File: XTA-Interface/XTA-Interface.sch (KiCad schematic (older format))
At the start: 23 parts, among them J1 IDE_CONNECTOR, J2 CF Adapter Power, J3 Bus_ISA_8bit, J4 Addresses, J5 Addresses, U1 BIOS FLASH, U2 74HCT245, U3 ATF/GAL22V10x-15, U4 DS1315, U5 AS6C4008-55PCN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

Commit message: WIP on XTA interface card.
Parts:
- removed BAT1: CR2032, Battery:BatteryHolder_Keystone_103_1x20mm, symbol Device:Battery_Cell
- removed C6: 0.1uF, Capacitor_THT:C_Disc_D6.0mm_W2.5mm_P5.00mm, symbol Device:C
- removed H1, H2, H3, H4: MountingHole_Pad, MountingHole:MountingHole_3.5mm_Pad, symbol Mechanical:MountingHole_Pad
- removed J2: CF Adapter Power, Connector_PinSocket_2.54mm:PinSocket_1x02_P2.54mm_Vertical, symbol Connector_Generic:Conn_01x02
- removed U4: DS1315, Package_DIP:DIP-16_W7.62mm_Socket, symbol 00Common:DS1315
- removed U5: AS6C4008-55PCN, Package_DIP:DIP-32_W15.24mm_Socket, symbol Memory_RAM:AS6C4008-55PCN
- removed Y1: 32.768 KHz, Crystal:Crystal_C38-LF_D3.0mm_L8.0mm_Horizontal, symbol Device:Crystal
- added J2: Drive Power, Connector_PinHeader_2.54mm:PinHeader_1x06_P2.54mm_Horizontal, symbol Connector_Generic:Conn_01x06
- added J6: LEDs, Connector_PinHeader_2.54mm:PinHeader_1x04_P2.54mm_Horizontal, symbol Connector_Generic:Conn_01x04
- added J7: XTA_CONNECTOR_1, Connector_PinHeader_2.54mm:PinHeader_2x20_P2.54mm_Vertical, symbol 00Common:XTA_CONNECTOR
- added R1: 1K, Resistor_SMD:R_1206_3216Metric, symbol Device:R
- added U4: 74LS14, Package_DIP:DIP-14_W7.62mm_Socket, symbol 74xx:74LS14
- added U5: 74LS00, Package_DIP:DIP-14_W7.62mm_Socket, symbol 74xx:74LS00
- C1, C2, C3, C4, C5: footprint Capacitor_THT:C_Disc_D6.0mm_W2.5mm_P5.00mm -> Capacitor_SMD:C_1206_3216Metric
- C6: renamed from C7; value 22uF -> 22uF 25v; footprint Capacitor_THT:CP_Radial_D5.0mm_P2.50mm -> Capacitor_Tantalum_SMD:CP_EIA-3528-15_AVX-H
- J1: value IDE_CONNECTOR -> XTA_CONNECTOR_0; footprint Connector_PinSocket_2.54mm:PinSocket_2x20_P2.54mm_Vertical -> Connector_PinHeader_2.54mm:PinHeader_2x20_P2.54mm_Vertical; symbol 00Common:IDE_CONNECTOR -> 00Common:XTA_CONNECTOR
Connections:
- net labels added: +12V, AEN, BIOS_SEL_JUMPER, IRQ2, IRQ5, ROM_ADDR_JUMPER_0, ROM_ADDR_JUMPER_1, XTA_DRQ, XTA_IRQ, ~CS_XTA0, ~CS_XTA1, ~DACK3, ~DRV_ACTIVE, ~XTA_DACK
- net labels removed: ATA_ADDR_JUMPER, ROM_ADDR_JUMPER, V20_JUMPER, XTAL1, XTAL2, ~CE~_BIOS_DECODE, ~CE~_BIOS_THRU, ~CS1~_ATA, ~IOR_OR_MEMR, ~IOR~_DELAYED, ~RESET
- wire segments 114 -> 186
- no-connect marks 39 -> 27
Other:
- note added: "0"
- note added: "1"
- note added: "1\n"
- note added: "OTHER HEADERS"
- note added: "Q"
- note added: "When ~R~ goes low, ~S~ also goes high, Q = 0\nIf ~R~ goes high, again, Q = 1\nIf ~DACK3~ is high but either of ~IOR~ or ~IOW~ go low, the state of the flop flop does not change?"
- note added: "XTA CONNECTOR"
- note added: "~R"
- note added: "~S"
- note removed: "CF ADAPTER"
- note removed: "REAL TIME CLOCK\n(OPTIONAL)"
- note removed: "TANDY 1000 SRAM\n(OPTIONAL)"
- moved on the sheet: C6

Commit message: WIP on XTA interface card.
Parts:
- removed C5: 0.1uF, Capacitor_SMD:C_1206_3216Metric, symbol Device:C
- removed U4: 74LS14, Package_DIP:DIP-14_W7.62mm_Socket, symbol 74xx:74LS14
- removed U5: 74LS00, Package_DIP:DIP-14_W7.62mm_Socket, symbol 74xx:74LS00
- added U4: ATF/GAL16V8-15, Package_DIP:DIP-20_W7.62mm_Socket, symbol 00Common:GAL16V8
- U3: value ATF/GAL22V10x-15 -> ATF/GAL16V8-15; footprint Package_DIP:DIP-24_W7.62mm_Socket -> Package_DIP:DIP-20_W7.62mm_Socket; symbol 00Common:GAL22V10 -> 00Common:GAL16V8
- renumbered C6 to C5
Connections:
- net +12V: now also J2.1 (Pin_1); no longer J2.5 (Pin_5)
- net A02: now also U3.3 (I3); no longer U3.1 (I1/CLK)
- net A03: now also U4.1 (I1/CLK); no longer U3.2 (I2)
- net A04: now also U4.2 (I2); no longer U3.3 (I3)
- net A05: now also U4.3 (I3); no longer U3.4 (I4)
- net A06: now also U4.4 (I4); no longer U3.5 (I5)
- net A07: now also U4.5 (I5); no longer U3.6 (I6)
- net A08: now also U4.6 (I6); no longer U3.7 (I7)
- net A09: now also U4.7 (I7); no longer U3.8 (I8)
- net A13: now also U3.4 (I4); no longer U3.9 (I9)
- net A14: now also U3.5 (I5); no longer U3.10 (I10)
- net A15: now also U3.6 (I6); no longer U3.11 (I11)
- net A16: now also U3.7 (I7); no longer U3.13 (I12)
- net A17: now also U3.8 (I8); no longer U3.14 (IO10)
- net A18: now also U3.9 (I9); no longer U3.15 (IO9)
- net A19: now also U3.11 (I10/~OE~); no longer U3.16 (IO8)
- net GND: now also J2.5 (Pin_5), U3.10 (GND), U4.10 (GND); no longer J2.4 (Pin_4), U3.12 (GND)
- net VCC: now also J2.3 (Pin_3), J2.4 (Pin_4), U3.20 (VCC), U4.20 (VCC); no longer J2.1 (Pin_1), U3.24 (VCC)
- net ~CE~_BIOS: now also U3.15 (IO5); no longer U3.19 (IO5)
- net ~CS_XTA0: now also U3.16 (IO4); no longer U3.20 (IO4)
- net ~CS_XTA1: now also U3.17 (I03); no longer U3.21 (I03)
- net ~DACK3: now also U4.11 (I10/~OE~)
- net ~IOR: now also U4.9 (I9)
- net ~IOW: now also U4.8 (I8)
- net ~MEMR: now also U3.13 (IO7); no longer U3.17 (IO7)
- net ~MEMR~_DELAYED: now also U3.14 (IO6); no longer U3.18 (IO6)
- net ~XTA_DACK: now also U4.12 (IO8)
- net BIOS_SEL_JUMPER renamed ST_WD_JUMPER
- net ST_WD_JUMPER: now also U3.2 (I2)
- net ROM_ADDR_JUMPER_0 renamed ADDR_JUMPER_0
- net ADDR_JUMPER_0: now also U3.19 (IO1); no longer U3.23 (IO1)
- net ROM_ADDR_JUMPER_1 renamed ADDR_JUMPER_1
- net ADDR_JUMPER_1: now also U3.18 (IO2); no longer U3.22 (IO2)
- new net DECODE_IO_RANGE: U3.1 (I1/CLK), U4.13 (IO7)
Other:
- note added: "DECODING AND GLUE"
- note added: "Spare for extra\ndelay if needed."
- note added: "Unused pins are for\nadding propogation\ndelay. Need at least 4."
- note removed: "0"
- note removed: "1"
- note removed: "1\n"
- note removed: "DECODING"
- note removed: "Q"
- note removed: "When ~R~ goes low, ~S~ also goes high, Q = 0\nIf ~R~ goes high, again, Q = 1\nIf ~DACK3~ is high but either of ~IOR~ or ~IOW~ go low, the state of the flop flop does not change?"
- note removed: "~R"
- note removed: "~S"
- moved on the sheet: U2

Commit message: More WIP on XTA interface card.
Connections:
- net A19: now also U3.14 (IO6); no longer U3.11 (I10/~OE~)
- net ADDR_JUMPER_0: now also U3.11 (I10/~OE~); no longer U3.19 (IO1)
- net ADDR_JUMPER_1: now also U3.12 (IO8); no longer U3.18 (IO2)
- net ~CE~_BIOS: now also U3.18 (IO2); no longer U3.15 (IO5)
- net ~CS_XTA0: now also U3.17 (I03); no longer U3.16 (IO4)
- net ~CS_XTA1: now also U3.16 (IO4); no longer U3.17 (I03)
- net ~MEMR: now also U3.15 (IO5); no longer U3.13 (IO7)
- net ~MEMR~_DELAYED: now also U3.19 (IO1); no longer U3.14 (IO6)
- net XTA_DRQ renamed DRQ3
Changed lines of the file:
@@
 Text GLabel 7900 4300 2    50   Input ~ 0
 D7_BUF
-Text GLabel 5250 1650 2    39   Input ~ 0
+Text GLabel 5250 1550 2    39   Input ~ 0
 ~CS_XTA0
-Text GLabel 5250 1750 2    39   Input ~ 0
+Text GLabel 5250 1450 2    39   Input ~ 0
 ~CE~_BIOS
 Text GLabel 2600 3400 2    50   Input ~ 0
@@
 Text GLabel 2600 2500 2    50   Input ~ 0
 A15
-Text GLabel 4250 2250 0    50   Input ~ 0
+Text GLabel 5250 1850 2    50   Input ~ 0
 A19
 Text GLabel 4250 2150 0    50   Input ~ 0
@@
 Text GLabel 4150 5950 0    50   Input ~ 0
 D0
-Text GLabel 5550 950  0    50   Input ~ 0
+Text GLabel 3850 2350 3    50   Input ~ 0
 ADDR_JUMPER_0
-Text GLabel 5550 850  0    50   Input ~ 0
+Text GLabel 5400 2300 3    50   Input ~ 0
 ADDR_JUMPER_1
 $Comp
@@
 XTA_IRQ
 Text GLabel 9450 2350 0    50   Input ~ 0
-XTA_DRQ
+DRQ3
 Text GLabel 9450 2250 0    39   Input ~ 0
 ~XTA_DACK
@@
 XTA_IRQ
 Text GLabel 9450 5200 0    50   Input ~ 0
-XTA_DRQ
+DRQ3
 Text GLabel 9450 5100 0    39   Input ~ 0
 ~XTA_DACK
@@
 Text GLabel 4150 6850 0    39   Input ~ 0
 ~MEMR
-Text GLabel 5250 1550 2    39   Input ~ 0
+Text GLabel 5250 1650 2    39   Input ~ 0
 ~CS_XTA1
 Text GLabel 4000 3350 0    50   Input ~ 0
@@
 Text GLabel 4250 1750 0    50   Input ~ 0
 A14
-Text GLabel 5250 1850 2    39   Input ~ 0
+Text GLabel 5250 1350 2    39   Input ~ 0
 ~MEMR~_DELAYED
-Text GLabel 5250 1950 2    39   Input ~ 0
+Text GLabel 5250 1750 2    39   Input ~ 0
 ~MEMR
 $Comp
@@
 	2500 2000 2600 2000
 Text GLabel 1000 2500 0    50   Input ~ 0
-XTA_DRQ
+DRQ3
 Text GLabel 1000 2400 0    39   Input ~ 0
 ~DACK3
@@
 Text GLabel 5000 4050 2    39   Input ~ 0
 ~XTA_DACK
-NoConn ~ 5250 2050
+NoConn ~ 5250 1950
 NoConn ~ 5000 3450
 NoConn ~ 5000 3350
@@
 Wire Wire Line
 	3700 950  3850 950
-Wire Wire Line
-	5250 1350 5650 1350
-Wire Wire Line
-	5650 1350 5650 950
-Wire Wire Line
-	5650 950  5550 950
-Wire Wire Line
-	5550 850  5750 850
-Wire Wire Line
-	5750 850  5750 1450
-Wire Wire Line
-	5750 1450 5250 1450
-Text Notes 5150 2250 0    50   ~ 0
+Text Notes 2950 2200 0    50   ~ 0
 Spare for extra\ndelay if needed.
 Text Notes 4900 4350 0    50   ~ 0
 Unused pins are for\nadding propogation\ndelay. Need at least 4.
+Wire Wire Line
+	5250 2050 5400 2050
+Wire Wire Line
+	5400 2050 5400 2300
+Wire Wire Line
+	4250 2250 3850 2250
+Wire Wire Line
+	3850 2250 3850 2350
 $EndSCHEMATC

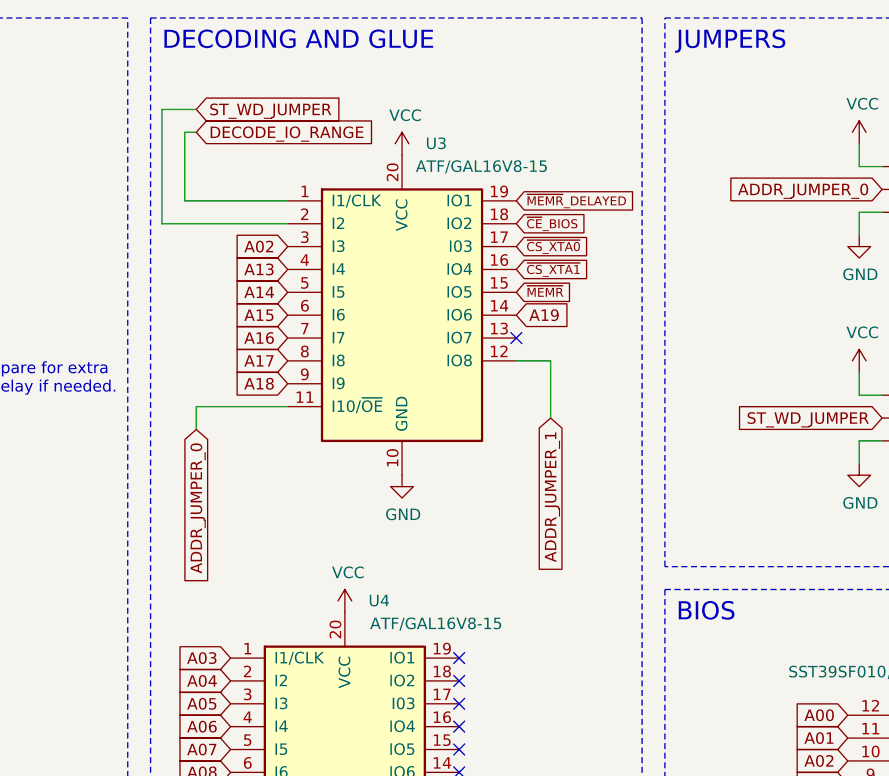
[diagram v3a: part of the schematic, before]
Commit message: XTA interface WIP. All items connected - still needs a bunch of cleanup.
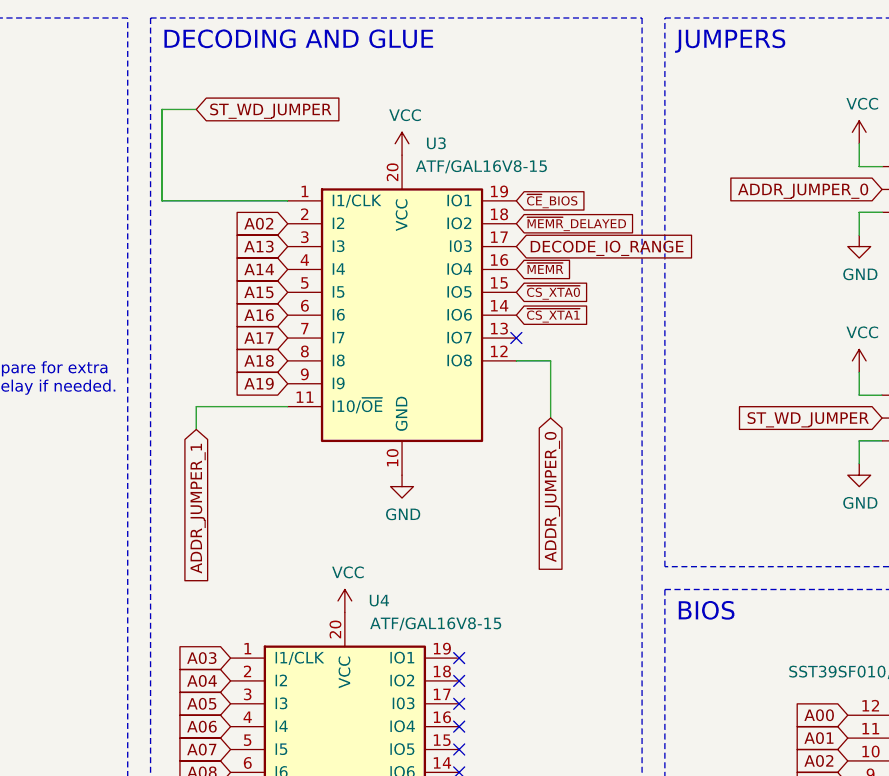
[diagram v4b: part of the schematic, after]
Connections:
- net A02: now also U3.2 (I2); no longer U3.3 (I3)
- net A13: now also U3.3 (I3); no longer U3.4 (I4)
- net A14: now also U3.4 (I4); no longer U3.5 (I5)
- net A15: now also U3.5 (I5); no longer U3.6 (I6)
- net A16: now also U3.6 (I6); no longer U3.7 (I7)
- net A17: now also U3.7 (I7); no longer U3.8 (I8)
- net A18: now also U3.8 (I8); no longer U3.9 (I9)
- net A19: now also U3.9 (I9); no longer U3.14 (IO6)
- net ADDR_JUMPER_0: now also U3.12 (IO8); no longer U3.11 (I10/~OE~)
- net ADDR_JUMPER_1: now also U3.11 (I10/~OE~); no longer U3.12 (IO8)
- net DECODE_IO_RANGE: now also U3.17 (I03); no longer U3.1 (I1/CLK)
- net ST_WD_JUMPER: now also U3.1 (I1/CLK); no longer U3.2 (I2)
- net ~CE~_BIOS: now also U3.19 (IO1); no longer U3.18 (IO2)
- net ~CS_XTA0: now also U3.15 (IO5); no longer U3.17 (I03)
- net ~CS_XTA1: now also U3.14 (IO6); no longer U3.16 (IO4)
- net ~MEMR: now also U3.16 (IO4); no longer U3.15 (IO5)
- net ~MEMR~_DELAYED: now also U3.18 (IO2); no longer U3.19 (IO1)
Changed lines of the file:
@@
 Text GLabel 7900 4300 2    50   Input ~ 0
 D7_BUF
-Text GLabel 5250 1550 2    39   Input ~ 0
+Text GLabel 5250 1750 2    39   Input ~ 0
 ~CS_XTA0
-Text GLabel 5250 1450 2    39   Input ~ 0
+Text GLabel 5250 1350 2    39   Input ~ 0
 ~CE~_BIOS
 Text GLabel 2600 3400 2    50   Input ~ 0
@@
 Text GLabel 2600 2500 2    50   Input ~ 0
 A15
-Text GLabel 5250 1850 2    50   Input ~ 0
+Text GLabel 4250 2150 0    50   Input ~ 0
 A19
-Text GLabel 4250 2150 0    50   Input ~ 0
+Text GLabel 4250 2050 0    50   Input ~ 0
 A18
-Text GLabel 4250 2050 0    50   Input ~ 0
+Text GLabel 4250 1950 0    50   Input ~ 0
 A17
-Text GLabel 4250 1950 0    50   Input ~ 0
+Text GLabel 4250 1850 0    50   Input ~ 0
 A16
-Text GLabel 4250 1850 0    50   Input ~ 0
+Text GLabel 4250 1750 0    50   Input ~ 0
 A15
 Connection ~ 6100 5400
@@
 Text GLabel 4150 5950 0    50   Input ~ 0
 D0
+Text GLabel 5400 2300 3    50   Input ~ 0
+ADDR_JUMPER_0
 Text GLabel 3850 2350 3    50   Input ~ 0
-ADDR_JUMPER_0
-Text GLabel 5400 2300 3    50   Input ~ 0
 ADDR_JUMPER_1
 $Comp
@@
 Text GLabel 4150 6850 0    39   Input ~ 0
 ~MEMR
-Text GLabel 5250 1650 2    39   Input ~ 0
+Text GLabel 5250 1850 2    39   Input ~ 0
 ~CS_XTA1
 Text GLabel 4000 3350 0    50   Input ~ 0
 A03
+Text GLabel 4250 1450 0    50   Input ~ 0
+A02
 Text GLabel 4250 1550 0    50   Input ~ 0
-A02
+A13
 Text GLabel 4250 1650 0    50   Input ~ 0
-A13
-Text GLabel 4250 1750 0    50   Input ~ 0
 A14
-Text GLabel 5250 1350 2    39   Input ~ 0
+Text GLabel 5250 1450 2    39   Input ~ 0
 ~MEMR~_DELAYED
-Text GLabel 5250 1750 2    39   Input ~ 0
+Text GLabel 5250 1650 2    39   Input ~ 0
 ~MEMR
 $Comp
@@
 Text GLabel 5000 3950 2    50   Input ~ 0
 DECODE_IO_RANGE
-Text GLabel 3850 1050 2    50   Input ~ 0
+Text GLabel 5250 1550 2    50   Input ~ 0
 DECODE_IO_RANGE
 $Comp
@@
 NoConn ~ 5000 3550
 Wire Wire Line
-	4250 1350 3800 1350
-Wire Wire Line
-	3800 1350 3800 1050
-Wire Wire Line
-	3800 1050 3850 1050
-Wire Wire Line
-	4250 1450 3700 1450
-Wire Wire Line
-	3700 1450 3700 950
-Wire Wire Line
 	3700 950  3850 950
 Text Notes 2950 2200 0    50   ~ 0
@@
 Wire Wire Line
 	3850 2250 3850 2350
+Wire Wire Line
+	4250 1350 3700 1350
+Wire Wire Line
+	3700 1350 3700 950
 $EndSCHEMATC

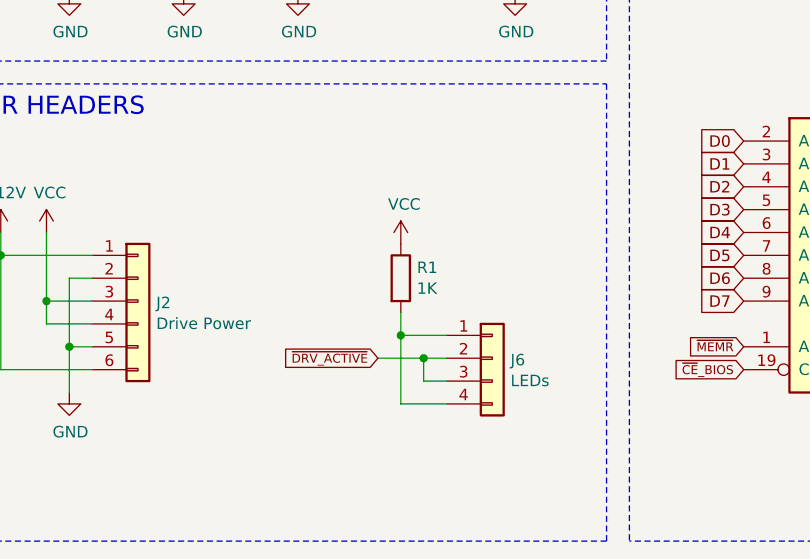
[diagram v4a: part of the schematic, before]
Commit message: WIP on XTA interface layout.
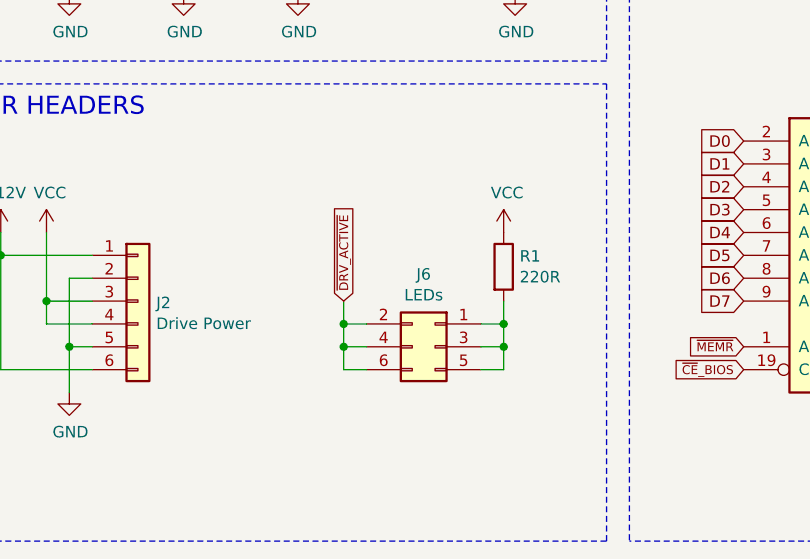
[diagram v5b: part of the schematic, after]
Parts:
- removed J6: LEDs, Connector_PinHeader_2.54mm:PinHeader_1x04_P2.54mm_Horizontal, symbol Connector_Generic:Conn_01x04
- added J6: LEDs, Connector_PinHeader_2.54mm:PinHeader_2x03_P2.54mm_Vertical, symbol Connector_Generic:Conn_02x03_Odd_Even
- R1: value 1K -> 220R
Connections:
- net ~DRV_ACTIVE: now also J6.2 (Pin_2), J6.4 (Pin_4), J6.6 (Pin_6)
- net at R1.2: now also J6.1 (Pin_1), J6.3 (Pin_3), J6.5 (Pin_5)
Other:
- moved on the sheet: R1
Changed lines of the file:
@@
 L Device:R R1
 U 1 1 6153EA2A
-P 2650 6550
-F 0 "R1" H 2720 6596 50  0000 L CNN
-F 1 "1K" H 2720 6505 50  0000 L CNN
-F 2 "Resistor_SMD:R_1206_3216Metric" V 2580 6550 50  0001 C CNN
-F 3 "~" H 2650 6550 50  0001 C CNN
-	1    2650 6550
+P 3100 6500
+F 0 "R1" H 3170 6546 50  0000 L CNN
+F 1 "220R" H 3170 6455 50  0000 L CNN
+F 2 "Resistor_SMD:R_1206_3216Metric" V 3030 6500 50  0001 C CNN
+F 3 "~" H 3100 6500 50  0001 C CNN
+	1    3100 6500
 	1    0    0    -1
 $EndComp
@@
 L power:VCC #PWR05
 U 1 1 6153F2F8
-P 2650 6400
-F 0 "#PWR05" H 2650 6250 50  0001 C CNN
-F 1 "VCC" H 2665 6573 50  0000 C CNN
-F 2 "" H 2650 6400 50  0001 C CNN
-F 3 "" H 2650 6400 50  0001 C CNN
-	1    2650 6400
+P 3100 6350
+F 0 "#PWR05" H 3100 6200 50  0001 C CNN
+F 1 "VCC" H 3115 6523 50  0000 C CNN
+F 2 "" H 3100 6350 50  0001 C CNN
+F 3 "" H 3100 6350 50  0001 C CNN
+	1    3100 6350
 	1    0    0    -1
 $EndComp
-$Comp
-L Connector_Generic:Conn_01x04 J6
-U 1 1 6153FB55
-P 3050 6900
-F 0 "J6" H 3130 6892 50  0000 L CNN
-F 1 "LEDs" H 3130 6801 50  0000 L CNN
-F 2 "Connector_PinHeader_2.54mm:PinHeader_1x04_P2.54mm_Horizontal" H 3050 6900 50  0001 C CNN
-F 3 "~" H 3050 6900 50  0001 C CNN
-	1    3050 6900
-	1    0    0    -1
-$EndComp
-Wire Wire Line
-	2850 7100 2650 7100
-Wire Wire Line
-	2650 7100 2650 6800
-Wire Wire Line
-	2850 6800 2650 6800
-Connection ~ 2650 6800
-Wire Wire Line
-	2650 6800 2650 6700
-Text GLabel 2550 6900 0    39   Input ~ 0
+Text GLabel 2400 6650 1    39   Input ~ 0
 ~DRV_ACTIVE
-Wire Wire Line
-	2550 6900 2750 6900
-Wire Wire Line
-	2850 7000 2750 7000
-Wire Wire Line
-	2750 7000 2750 6900
-Connection ~ 2750 6900
-Wire Wire Line
-	2750 6900 2850 6900
 Text Notes 600  5850 0    79   ~ 0
 OTHER HEADERS
@@
 Wire Wire Line
 	3700 1350 3700 950
+$Comp
+L Connector_Generic:Conn_02x03_Odd_Even J6
+U 1 1 613F478C
+P 2800 6850
+F 0 "J6" H 2850 7167 50  0000 C CNN
+F 1 "LEDs" H 2850 7076 50  0000 C CNN
+F 2 "Connector_PinHeader_2.54mm:PinHeader_2x03_P2.54mm_Vertical" H 2800 6850 50  0001 C CNN
+F 3 "~" H 2800 6850 50  0001 C CNN
+	1    2800 6850
+	-1   0    0    -1
+$EndComp
+Wire Wire Line
+	2400 6650 2400 6750
+Wire Wire Line
+	2500 6850 2400 6850
+Wire Wire Line
+	2400 6850 2400 6750
+Connection ~ 2400 6750
+Wire Wire Line
+	2400 6750 2500 6750
+Wire Wire Line
+	2500 6950 2400 6950
+Wire Wire Line
+	2400 6950 2400 6850
+Connection ~ 2400 6850
+Wire Wire Line
+	3000 6750 3100 6750
+Wire Wire Line
+	3100 6750 3100 6650
+Wire Wire Line
+	3100 6750 3100 6850
+Wire Wire Line
+	3100 6950 3000 6950
+Connection ~ 3100 6750
+Wire Wire Line
+	3100 6850 3000 6850
+Connection ~ 3100 6850
+Wire Wire Line
+	3100 6850 3100 6950
 $EndSCHEMATC

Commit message: Silkscreen work for XTA interface.
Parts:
- CN1: renamed from J1; value XTA_CONNECTOR_0 -> DRIVE 0
- CN2: renamed from J7; value XTA_CONNECTOR_1 -> DRIVE 1
- JP1: renamed from J5; value Addresses -> Options
- U3: renamed from U4; value ATF/GAL16V8-15 -> ATF/GAL16V8-15 \"LEFT\"
- U4: renamed from U3; value ATF/GAL16V8-15 -> ATF/GAL16V8-15 \"RIGHT\"
- renumbered C4 to C3, C3 to C4, J6 to CN3, J2 to CN4, J4 to JP2
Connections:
- net ADDR_JUMPER_0: now also JP2.4 (Pin_4), U4.11 (I10/~OE~); no longer JP2.3 (Pin_3), U4.12 (IO8)
- net ADDR_JUMPER_1: now also JP2.3 (Pin_3), U4.12 (IO8); no longer JP2.4 (Pin_4), U4.11 (I10/~OE~)
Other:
- moved on the sheet: C3, C4, C5, CN3, CN4, JP1, JP2, R1
